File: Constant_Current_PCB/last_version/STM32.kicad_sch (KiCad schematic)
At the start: 16 parts, among them SW3 TS-1088-AR02016, U1 STM32L432KCU6, X1 MC-306 32.768kHz 6.0pF 20ppm

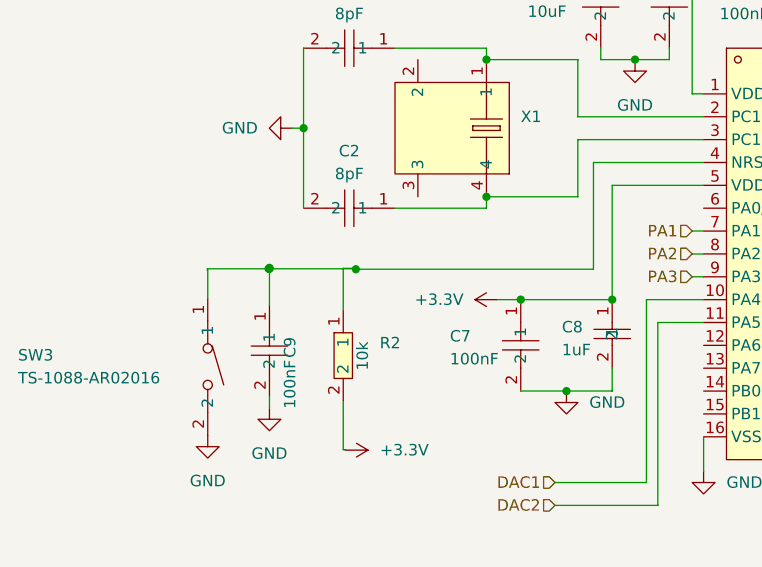
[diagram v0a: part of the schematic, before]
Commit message: fixed NRST
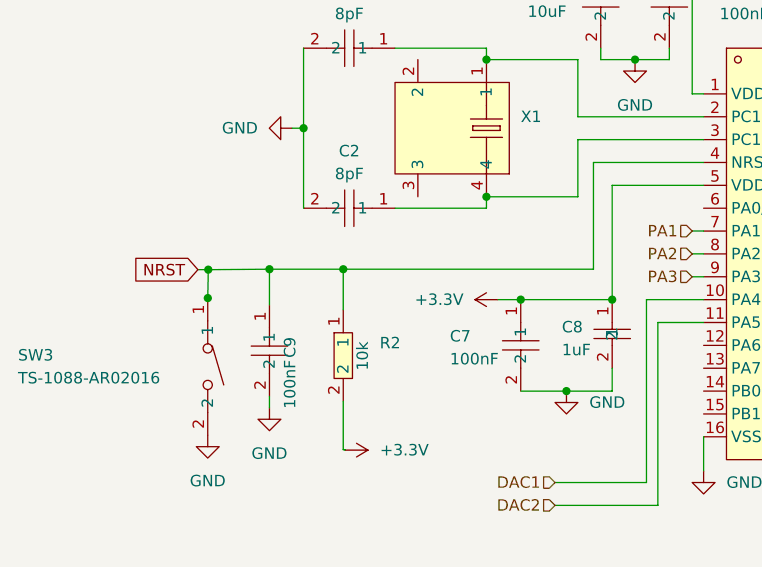
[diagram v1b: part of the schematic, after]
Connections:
- net NRST: now reaches C9.1, R2.1, SW3.1, U1.4 (NRST)
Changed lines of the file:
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@@
-	)
-	(junction
-		(at 43.208 65.15)
-		(diameter 0)
-		(color 0 0 0 0)
-	)
-	(junction
-		(at 52.8 65.2)
-		(diameter 0)
-		(color 0 0 0 0)
-	)
-	(junction
-		(at 43.2 65.05)
-		(diameter 0)
-		(color 0 0 0 0)
 	)
 	(junction
@@
 	)
 	(junction
-		(at 43.1 65.15)
+		(at 36.4 65.25)
 		(diameter 0)
 		(color 0 0 0 0)
@@
 	)
 	(junction
+		(at 36.35 68.408)
+		(diameter 0)
+		(color 0 0 0 0)
+	)
+	(junction
 		(at 148.59 83.82)
 		(diameter 0)
@@
 	)
 	(junction
+		(at 51.4 65.2)
+		(diameter 0)
+		(color 0 0 0 0)
+	)
+	(junction
 		(at 76.2 78.74)
 		(diameter 0)
@@
 	)
 	(junction
+		(at 43.2 65.2)
+		(diameter 0)
+		(color 0 0 0 0)
+	)
+	(junction
 		(at 87.63 30.48)
 		(diameter 0)
@@
 	(wire
 		(pts
+			(xy 35.25 65.25) (xy 36.4 65.25)
+		)
+		(stroke
+			(width 0)
+			(type default)
+		)
+	)
+	(wire
+		(pts
 			(xy 87.63 41.91) (xy 83.82 41.91)
 		)
@@
 	(wire
 		(pts
-			(xy 79.2 65.2) (xy 52.8 65.2)
+			(xy 36.35 65.2) (xy 36.4 65.25)
 		)
 		(stroke
@@
 	(wire
 		(pts
-			(xy 43.1 65.15) (xy 36.3 65.15)
-		)
-		(stroke
-			(width 0)
-			(type default)
-		)
-	)
-	(wire
-		(pts
 			(xy 81.28 78.74) (xy 76.2 78.74)
 		)
@@
 	(wire
 		(pts
+			(xy 36.35 68.408) (xy 36.35 68.45)
+		)
+		(stroke
+			(width 0)
+			(type default)
+		)
+	)
+	(wire
+		(pts
 			(xy 141.224 78.74) (xy 139.7 78.74)
 		)
@@
 	(wire
 		(pts
-			(xy 43.208 65.15) (xy 52.65 65.15)
-		)
-		(stroke
-			(width 0)
-			(type default)
-		)
-	)
-	(wire
-		(pts
 			(xy 85.09 88.9) (xy 74.93 88.9)
 		)
@@
 	(wire
 		(pts
-			(xy 52.8 65.1) (xy 52.8 65.2)
-		)
-		(stroke
-			(width 0)
-			(type default)
-		)
-	)
-	(wire
-		(pts
 			(xy 57.15 40.64) (xy 67.31 40.64)
 		)
@@
 	(wire
 		(pts
-			(xy 52.65 65.2) (xy 52.8 65.2)
-		)
-		(stroke
-			(width 0)
-			(type default)
-		)
-	)
-	(wire
-		(pts
-			(xy 43.208 65.15) (xy 43.208 65.05)
+			(xy 36.4 65.25) (xy 36.35 68.408)
 		)
 		(stroke
@@
 	(wire
 		(pts
-			(xy 43.2 65.05) (xy 43.2 69.17)
-		)
-		(stroke
-			(width 0)
-			(type default)
-		)
-	)
-	(wire
-		(pts
 			(xy 160.02 66.04) (xy 152.4 66.04)
 		)
@@
 	(wire
 		(pts
-			(xy 36.3 65.15) (xy 36.3 65.3)
-		)
-		(stroke
-			(width 0)
-			(type default)
-		)
-	)
-	(wire
-		(pts
 			(xy 72.39 30.48) (xy 80.01 30.48)
 		)
@@
 	(wire
 		(pts
+			(xy 43.2 65.2) (xy 51.4 65.2)
+		)
+		(stroke
+			(width 0)
+			(type default)
+		)
+	)
+	(wire
+		(pts
 			(xy 43.2 79.33) (xy 43.2 80.6)
 		)
@@
 	(wire
 		(pts
-			(xy 51.4 65.1) (xy 51.4 69.72)
-		)
-		(stroke
-			(width 0)
-			(type default)
-		)
-	)
-	(wire
-		(pts
 			(xy 80.01 30.48) (xy 87.63 30.48)
 		)
@@
 	(wire
 		(pts
+			(xy 51.4 65.2) (xy 79.2 65.2)
+		)
+		(stroke
+			(width 0)
+			(type default)
+		)
+	)
+	(wire
+		(pts
 			(xy 142.24 44.45) (xy 140.716 44.45)
 		)
@@
 	(wire
 		(pts
+			(xy 36.35 68.408) (xy 36.342 68.408)
+		)
+		(stroke
+			(width 0)
+			(type default)
+		)
+	)
+	(wire
+		(pts
 			(xy 77.47 50.8) (xy 91.44 50.8)
 		)
@@
 	(wire
 		(pts
-			(xy 43.2 65.05) (xy 43.208 65.05)
-		)
-		(stroke
-			(width 0)
-			(type default)
-		)
-	)
-	(wire
-		(pts
 			(xy 140.716 45.72) (xy 139.7 45.72)
 		)
@@
 	(wire
 		(pts
-			(xy 43.1 65.05) (xy 43.1 65.15)
-		)
-		(stroke
-			(width 0)
-			(type default)
-		)
-	)
-	(wire
-		(pts
 			(xy 91.44 68.58) (xy 85.09 68.58)
 		)
@@
 	(wire
 		(pts
-			(xy 36.3 65.3) (xy 36.342 65.3)
-		)
-		(stroke
-			(width 0)
-			(type default)
-		)
-	)
-	(wire
-		(pts
-			(xy 52.65 65.15) (xy 52.65 65.2)
-		)
-		(stroke
-			(width 0)
-			(type default)
-		)
-	)
-	(wire
-		(pts
 			(xy 67.31 41.91) (xy 77.47 41.91)
 		)
@@
 	(wire
 		(pts
+			(xy 36.4 65.25) (xy 43.2 65.2)
+		)
+		(stroke
+			(width 0)
+			(type default)
+		)
+	)
+	(wire
+		(pts
 			(xy 141.224 81.28) (xy 139.7 81.28)
 		)
@@
 	(wire
 		(pts
-			(xy 43.1 65.15) (xy 43.208 65.15)
-		)
-		(stroke
-			(width 0)
-			(type default)
-		)
-	)
-	(wire
-		(pts
 			(xy 67.31 57.15) (xy 77.47 57.15)
 		)
@@
 	(wire
 		(pts
-			(xy 52.8 65.1) (xy 51.4 65.1)
-		)
-		(stroke
-			(width 0)
-			(type default)
-		)
-	)
-	(wire
-		(pts
 			(xy 85.09 68.58) (xy 85.09 88.9)
 		)
@@
 	(wire
 		(pts
+			(xy 51.4 69.72) (xy 51.4 65.2)
+		)
+		(stroke
+			(width 0)
+			(type default)
+		)
+	)
+	(wire
+		(pts
 			(xy 139.7 48.26) (xy 156.21 48.26)
 		)
@@
 	(wire
 		(pts
-			(xy 36.342 65.3) (xy 36.342 68.408)
-		)
-		(stroke
-			(width 0)
-			(type default)
-		)
-	)
-	(wire
-		(pts
-			(xy 43.1 65.05) (xy 43.2 65.05)
-		)
-		(stroke
-			(width 0)
-			(type default)
-		)
-	)
-	(wire
-		(pts
 			(xy 79.2 53.34) (xy 91.44 53.34)
 		)
@@
 	(wire
 		(pts
+			(xy 43.2 69.17) (xy 43.2 65.2)
+		)
+		(stroke
+			(width 0)
+			(type default)
+		)
+	)
+	(wire
+		(pts
 			(xy 144.78 93.98) (xy 148.59 93.98)
 		)
@@
 		)
 	)
+	(global_label "NRST"
+		(shape input)
+		(at 35.25 65.25 180)
+		(fields_autoplaced yes)
+		(effects
+			(font
+				(size 1.27 1.27)
+			)
+			(justify right)
+		)
+		(property "Intersheetrefs" "${INTERSHEET_REFS}"
+			(at 27.4872 65.25 0)
+			(effects
+				(font
+					(size 1.27 1.27)
+				)
+				(justify right)
+				(hide yes)
+			)
+		)
+	)
